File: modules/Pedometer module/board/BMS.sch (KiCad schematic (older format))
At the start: 20 parts, among them IC1 DW01A, J5 Conn_01x02_Female, Q2 AO3401A, Q3 FS8205A, U4 TP4056

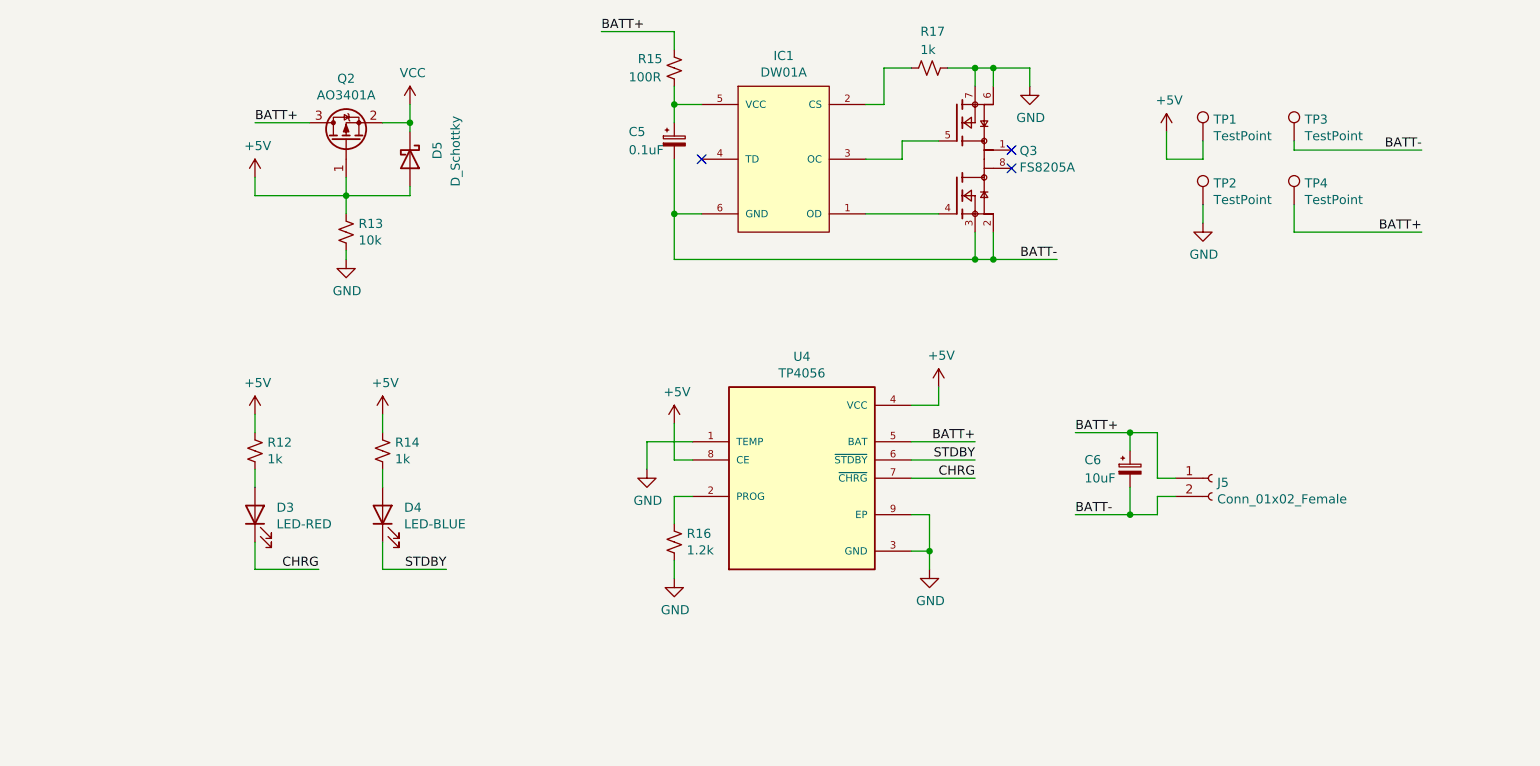
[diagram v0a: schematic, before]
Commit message: Pedometer module: Schematic and PCB layout
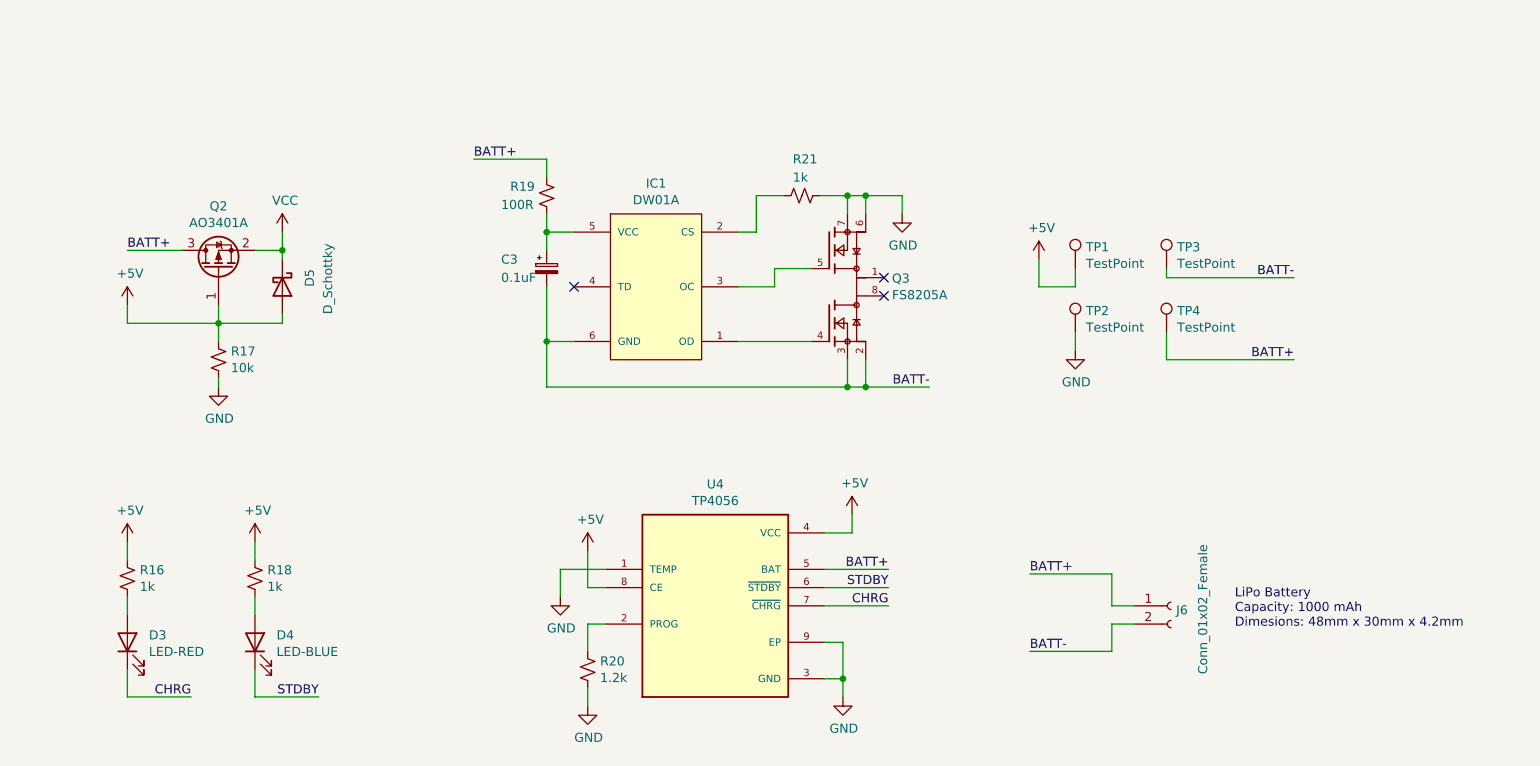
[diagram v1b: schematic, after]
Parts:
- removed C6: 10uF, Capacitor_SMD:C_0805_2012Metric_Pad1.18x1.45mm_HandSolder, symbol Device:CP_Small
- D5: footprint Diode_SMD:D_0805_2012Metric_Pad1.15x1.40mm_HandSolder -> Diode_SMD:D_SMA
- IC1: footprint board:SOT23-6 -> Package_TO_SOT_SMD:SOT-23-6_Handsoldering
- J6: renamed from J5; footprint Connector_PinSocket_2.54mm:PinSocket_1x02_P2.54mm_Vertical -> Board:SolderWire-SMD-BATT
- Q3: footprint board:SOP65P640X120-8N -> Board:SOP65P640X120-8N
- U4: footprint board:SOP127P600X175-9N -> Board:SOP127P600X175-9N
- renumbered C5 to C3, R12 to R16, R13 to R17, R14 to R18, R15 to R19, R16 to R20, R17 to R21
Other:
- note added: "LiPo Battery\nCapacity: 1000 mAh\nDimesions: 48mm x 30mm x 4.2mm"
- moved on the sheet: C3, D3, D4, D5, IC1, J6, Q2, Q3, R16, R17, R18, R19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

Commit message: Pedometer module: PCB size reduced
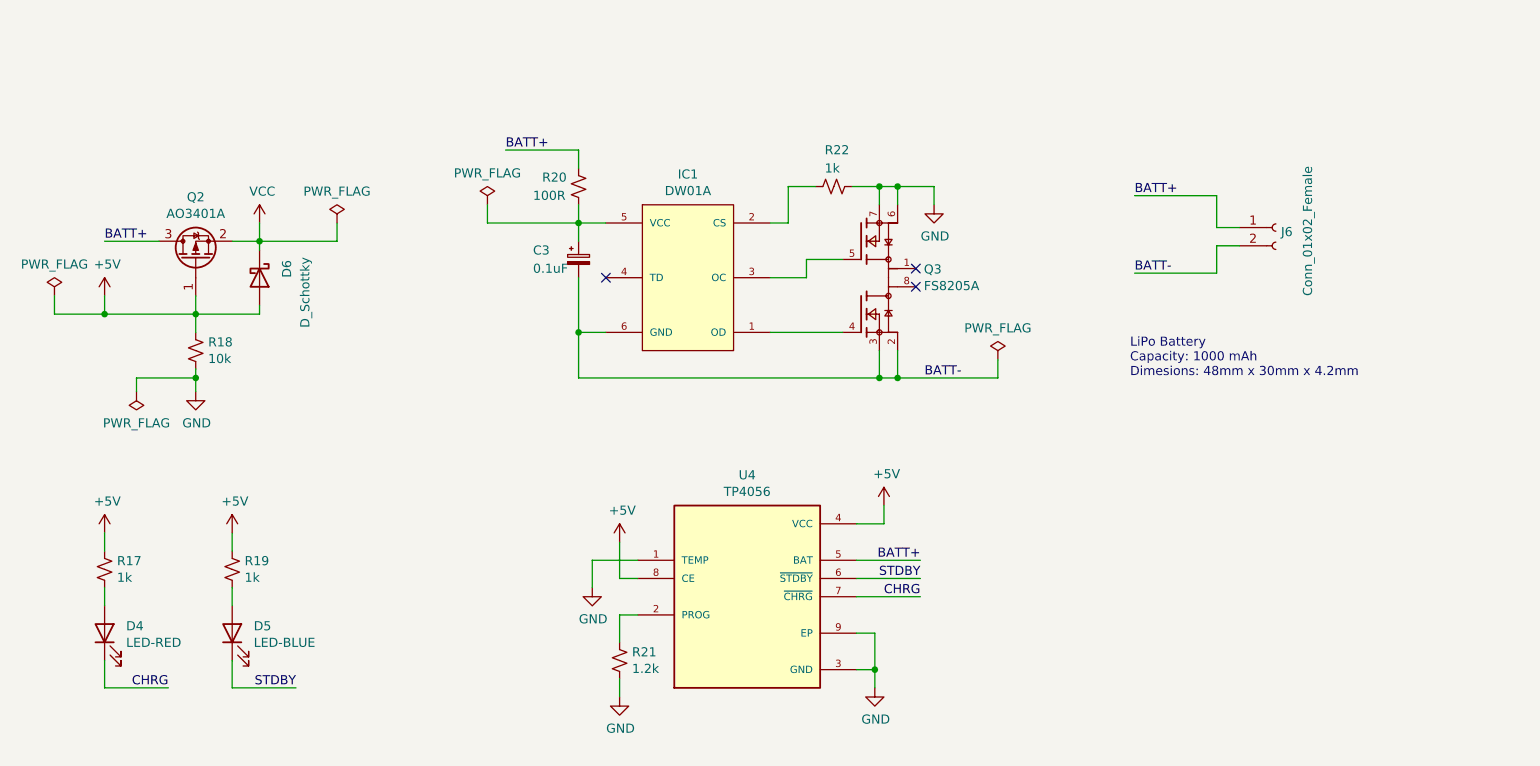
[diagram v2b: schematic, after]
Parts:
- removed TP1, TP2, TP3, TP4: TestPoint, TestPoint:TestPoint_Pad_1.5x1.5mm, symbol Connector:TestPoint
- J6: footprint Board:SolderWire-SMD-BATT -> Board:SolderWire_1x02_P2.00mm
- renumbered D3 to D4, D4 to D5, D5 to D6, R16 to R17, R17 to R18, R18 to R19, R19 to R20, R20 to R21, R21 to R22
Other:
- moved on the sheet: C3, D4, D5, D6, IC1, J6, Q2, Q3, R17, R18, R19, R20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

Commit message: Pedometer module: PCB modular
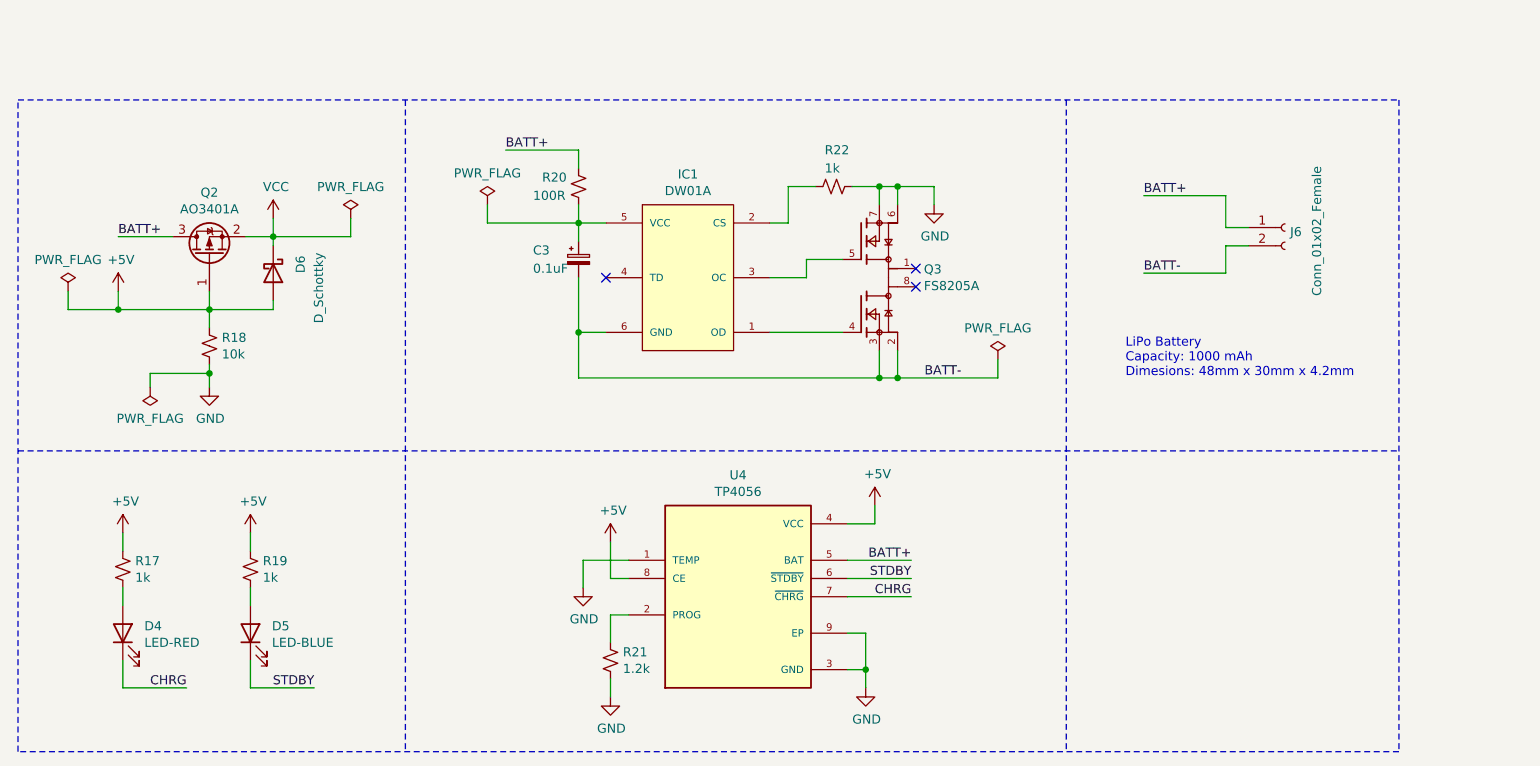
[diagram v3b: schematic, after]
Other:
- moved on the sheet: D4, D5, D6, J6, Q2, R17, R18, R19, R21, U4

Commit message: PCB: IMU
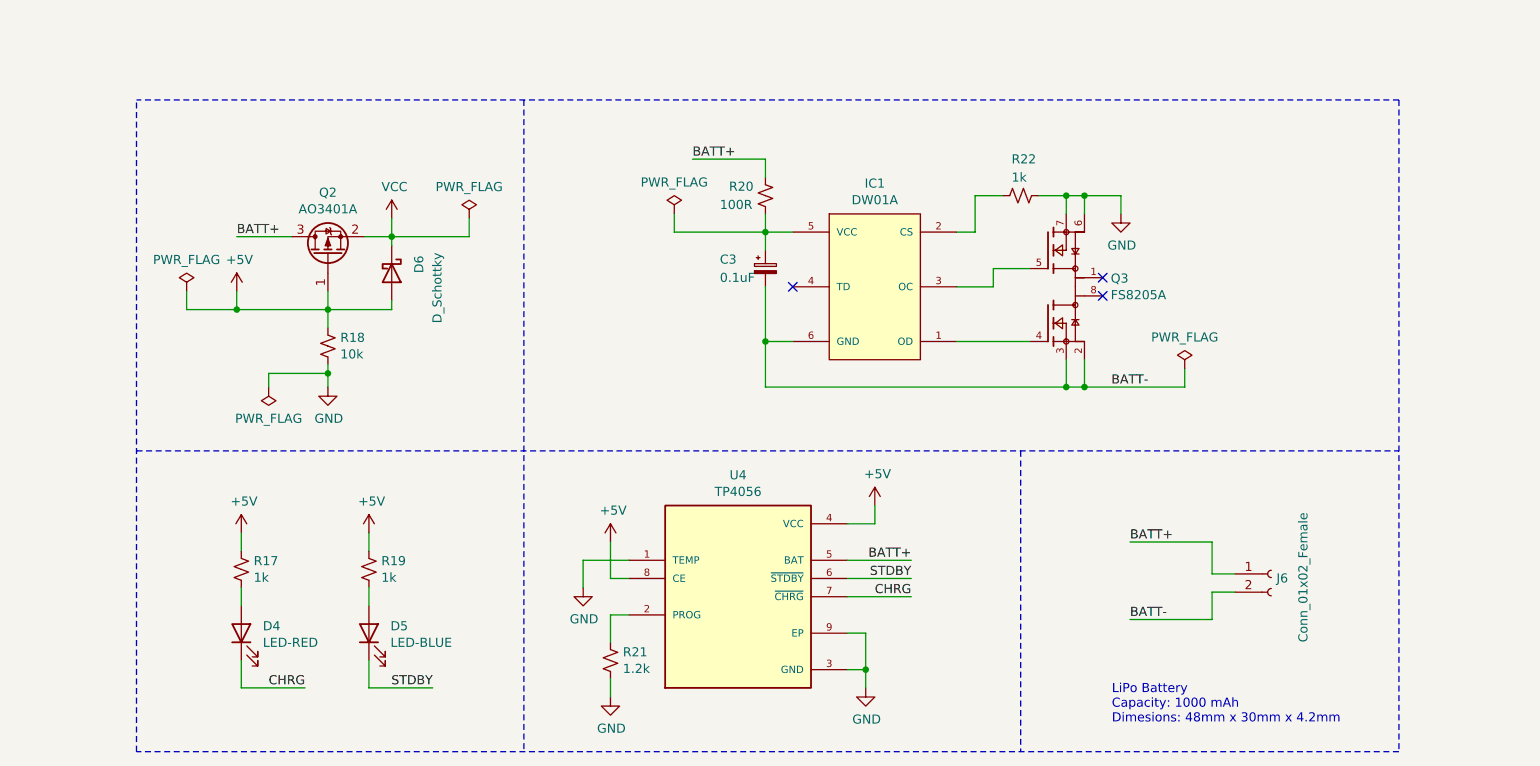
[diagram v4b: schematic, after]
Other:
- moved on the sheet: C3, D4, D5, D6, IC1, J6, Q2, Q3, R17, R18, R19, R20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
